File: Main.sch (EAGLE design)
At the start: 18 parts, among them X1 736880-49, X2 736880-49

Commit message: [rm]いったん全部消去
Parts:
- removed C1, C2, C3, C4, C5, C6: (no value), capacitor-wima:C10/5
- removed R1, R2, R3, R4, R5, R6: (no value), rcl:R-EU_0207/5V
- removed TR1, TR2: 166L8, trafo-hammondmfg:166L8
- removed V1, V2: (no value), VacuumTube:6BQ5-P
- removed X1, X2: 736880-49, con-conrad:736880-49
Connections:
- removed net GND: C2.2, C4.2, C5.2, C6.2, R1.1, R2.1, R3.1, R5.1
- removed net N$1: C2.1, R5.2, V2G$1.PK
- removed net N$12: C1.1, X2.2
- removed net N$2: C6.1, R6.2, V2G$1.PSG
- removed net N$3: C3.2, R2.2, V1G$1.PG
- removed net N$4: C1.2, R1.2, V2G$1.PG
- removed net N$5: TR2.BLK@1, V1G$1.PA
- removed net N$6: TR1.BLK@1, V2G$1.PA
- removed net N$7: C3.1, X1.2
- removed net N$8: C4.1, R3.2, V1G$1.PK
- removed net N$9: C5.1, R4.2, V1G$1.PSG
- removed net VCC: R4.1, R6.1, TR1.BLK@2, TR2.BLK@2

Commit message: [add]全回路作成
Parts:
- added C1, C2, C3, C6, C7, C8: 0.1u, VacuumTube:C
- added C10, C5: 10u, VacuumTube:C
- added C4, C9: 170, VacuumTube:C
- added JP1, JP2, JP3, JP4, JP5, JP6: (no value), VacuumTube:PINHD-1X2
- added R1, R10, R16, R7: 220k, VacuumTube:RESISTOR2
- added R11, R2: 3.83k, VacuumTube:RESISTOR2
- added R12, R3: 50k, VacuumTube:RESISTOR2
- added R13, R4: 1M, VacuumTube:RESISTOR2
- added R14, R5: 1.5k, VacuumTube:RESISTOR2
- added R15, R6: 100k, VacuumTube:RESISTOR2
- added R17, R8: 220u, VacuumTube:RESISTOR2
- added R18, R9: 2k, VacuumTube:RESISTOR2
- added V1, V3: (no value), VacuumTube:AT-MT9P(12AX7)
- added V2, V4: (no value), VacuumTube:AT-MT9P(6BQ5)
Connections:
- new net GND: C10.2, C4.2, C5.2, C9.2, JP1.1, JP2.1, JP3.1, JP4.1, R1.1, R10.1, R11.1, R15.1, R16.2, R17.2, R2.1, R6.1, R7.2, R8.2, V1C.H2, V2B.H2, V3C.H2, V4B.H2
- new net N$1: R3.1, V1A.TA
- new net N$10: C2.1
- new net N$11: V1C.H3, V3C.H3
- new net N$12: C3.1
- new net N$13: C3.2, R7.1, V2A.PG
- new net N$14: C4.1, R8.1, V2A.PK
- new net N$15: V2A.PA
- new net N$16: JP5.1
- new net N$17: C5.1, R9.1, V2A.PSG
- new net N$18: JP6.1
- new net N$19: R12.1, V3A.TA
- new net N$2: R2.2, V1A.TK
- new net N$20: R11.2, V3A.TK
- new net N$21: C6.2, R10.2, V3A.TG
- new net N$22: C6.1
- new net N$23: R14.2, V3B.TK
- new net N$24: R13.1, R14.1, R15.2
- new net N$25: C7.2, R13.2, V3B.TG
- new net N$26: C7.1
- new net N$27: C8.1
- new net N$28: C8.2, R16.1, V4A.PG
- new net N$29: C9.1, R17.1, V4A.PK
- new net N$3: JP2.2
- new net N$30: V4A.PA
- new net N$31: C10.1, R18.1, V4A.PSG
- new net N$4: JP1.2
- new net N$5: C1.2, R1.2, V1A.TG
- new net N$6: R5.2, V1B.TK
- new net N$7: C1.1
- new net N$8: R4.1, R5.1, R6.2
- new net N$9: C2.2, R4.2, V1B.TG
- new net VCC: JP3.2, JP5.2, JP6.2, R12.2, R18.2, R3.2, R9.2, V1B.TA, V3B.TA
- new net VCC/2: JP4.2, V1C.H1, V2B.H1, V3C.H1, V4B.H1
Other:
- note added: "FIRST_OUT1"
- note added: "FIRST_OUT2"
- note added: "INPUT1"
- note added: "INPUT2"
- note added: "SECOND_OUT1"
- note added: "SECOND_OUT2"
- note added: "THIRD_OUT1"
- note added: "THIRD_OUT2"

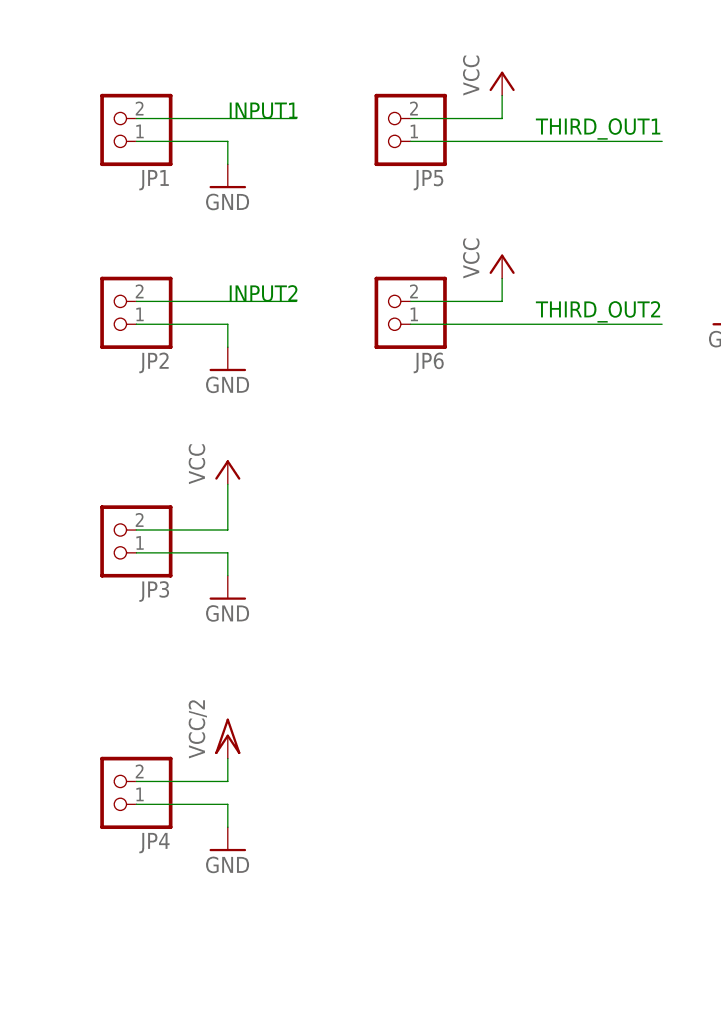
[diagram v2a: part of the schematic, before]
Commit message: [fix]ピンのラベルを編集
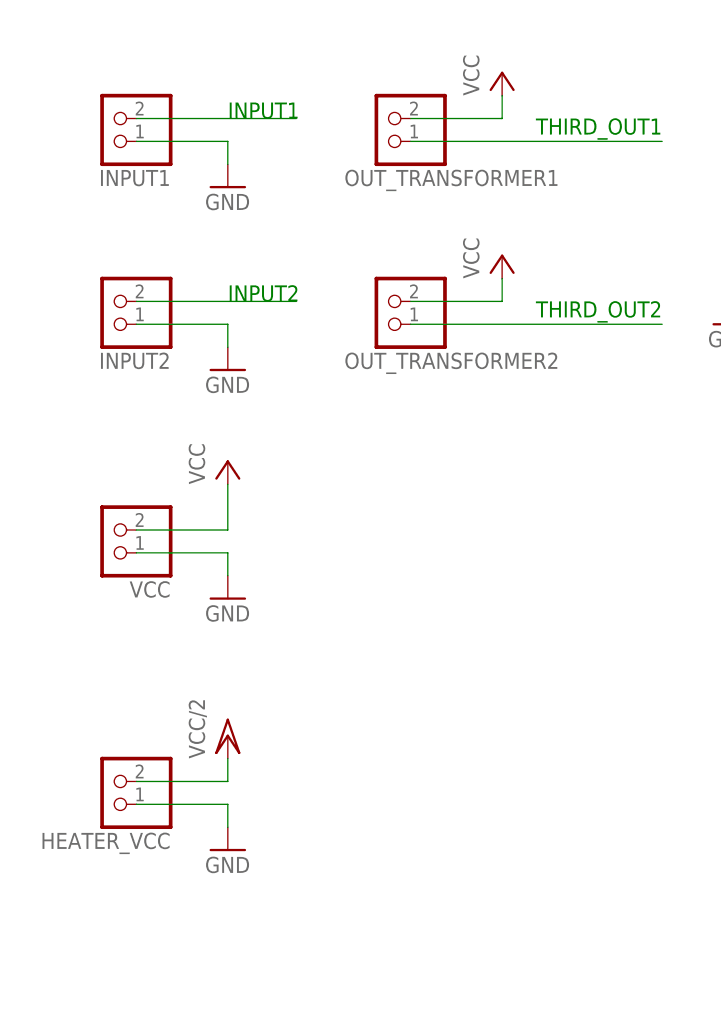
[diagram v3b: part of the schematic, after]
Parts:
- renumbered JP1 to INPUT1, JP2 to INPUT2, JP3 to VCC, JP4 to HEATER_VCC, JP5 to OUT_TRANSFORMER1, JP6 to OUT_TRANSFORMER2
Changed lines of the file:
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@@
 </classes>
 <parts>
-<part name="JP1" library="VacuumTube" library_urn="urn:adsk.eagle:library:8044196" deviceset="PINHD-1X2" device="" package3d_urn="urn:adsk.eagle:package:22435/2"/>
-<part name="JP2" library="VacuumTube" library_urn="urn:adsk.eagle:library:8044196" deviceset="PINHD-1X2" device="" package3d_urn="urn:adsk.eagle:package:22435/2"/>
+<part name="INPUT1" library="VacuumTube" library_urn="urn:adsk.eagle:library:8044196" deviceset="PINHD-1X2" device="" package3d_urn="urn:adsk.eagle:package:22435/2"/>
+<part name="INPUT2" library="VacuumTube" library_urn="urn:adsk.eagle:library:8044196" deviceset="PINHD-1X2" device="" package3d_urn="urn:adsk.eagle:package:22435/2"/>
 <part name="GND1" library="VacuumTube" library_urn="urn:adsk.eagle:library:8044196" deviceset="GND" device=""/>
 <part name="GND2" library="VacuumTube" library_urn="urn:adsk.eagle:library:8044196" deviceset="GND" device=""/>
-<part name="JP3" library="VacuumTube" library_urn="urn:adsk.eagle:library:8044196" deviceset="PINHD-1X2" device="" package3d_urn="urn:adsk.eagle:package:22435/2"/>
+<part name="VCC" library="VacuumTube" library_urn="urn:adsk.eagle:library:8044196" deviceset="PINHD-1X2" device="" package3d_urn="urn:adsk.eagle:package:22435/2"/>
 <part name="GND3" library="VacuumTube" library_urn="urn:adsk.eagle:library:8044196" deviceset="GND" device=""/>
 <part name="P+1" library="VacuumTube" library_urn="urn:adsk.eagle:library:8044196" deviceset="VCC" device=""/>
-<part name="JP4" library="VacuumTube" library_urn="urn:adsk.eagle:library:8044196" deviceset="PINHD-1X2" device="" package3d_urn="urn:adsk.eagle:package:22435/2"/>
+<part name="HEATER_VCC" library="VacuumTube" library_urn="urn:adsk.eagle:library:8044196" deviceset="PINHD-1X2" device="" package3d_urn="urn:adsk.eagle:package:22435/2"/>
 <part name="GND4" library="VacuumTube" library_urn="urn:adsk.eagle:library:8044196" deviceset="GND" device=""/>
 <part name="P+2" library="VacuumTube" library_urn="urn:adsk.eagle:library:8044196" deviceset="VCC/2" device=""/>
@@
 <part name="P+8" library="VacuumTube" library_urn="urn:adsk.eagle:library:8044196" deviceset="VCC" device=""/>
 <part name="GND13" library="VacuumTube" library_urn="urn:adsk.eagle:library:8044196" deviceset="GND" device=""/>
-<part name="JP5" library="VacuumTube" library_urn="urn:adsk.eagle:library:8044196" deviceset="PINHD-1X2" device="" package3d_urn="urn:adsk.eagle:package:22435/2"/>
+<part name="OUT_TRANSFORMER1" library="VacuumTube" library_urn="urn:adsk.eagle:library:8044196" deviceset="PINHD-1X2" device="" package3d_urn="urn:adsk.eagle:package:22435/2"/>
 <part name="P+9" library="VacuumTube" library_urn="urn:adsk.eagle:library:8044196" deviceset="VCC" device=""/>
 <part name="R9" library="VacuumTube" library_urn="urn:adsk.eagle:library:8044196" deviceset="RESISTOR2" device="" package3d_urn="urn:adsk.eagle:package:8969348/1" value="2k"/>
-<part name="JP6" library="VacuumTube" library_urn="urn:adsk.eagle:library:8044196" deviceset="PINHD-1X2" device="" package3d_urn="urn:adsk.eagle:package:22435/2"/>
+<part name="OUT_TRANSFORMER2" library="VacuumTube" library_urn="urn:adsk.eagle:library:8044196" deviceset="PINHD-1X2" device="" package3d_urn="urn:adsk.eagle:package:22435/2"/>
 <part name="P+10" library="VacuumTube" library_urn="urn:adsk.eagle:library:8044196" deviceset="VCC" device=""/>
 <part name="GND14" library="VacuumTube" library_urn="urn:adsk.eagle:library:8044196" deviceset="GND" device=""/>
@@
 </plain>
 <instances>
-<instance part="JP1" gate="G$1" x="0" y="93.98" smashed="yes" rot="R180">
+<instance part="INPUT1" gate="G$1" x="0" y="93.98" smashed="yes" rot="R180">
 <attribute name="NAME" x="6.35" y="88.265" size="1.778" layer="95" rot="R180"/>
 <attribute name="VALUE" x="6.35" y="99.06" size="1.778" layer="96" rot="R180"/>
 </instance>
-<instance part="JP2" gate="G$1" x="0" y="73.66" smashed="yes" rot="R180">
+<instance part="INPUT2" gate="G$1" x="0" y="73.66" smashed="yes" rot="R180">
 <attribute name="NAME" x="6.35" y="67.945" size="1.778" layer="95" rot="R180"/>
 <attribute name="VALUE" x="6.35" y="78.74" size="1.778" layer="96" rot="R180"/>
@@
 <attribute name="VALUE" x="10.16" y="63.5" size="1.778" layer="96"/>
 </instance>
-<instance part="JP3" gate="G$1" x="0" y="48.26" smashed="yes" rot="R180">
+<instance part="VCC" gate="G$1" x="0" y="48.26" smashed="yes" rot="R180">
 <attribute name="NAME" x="6.35" y="42.545" size="1.778" layer="95" rot="R180"/>
 <attribute name="VALUE" x="6.35" y="53.34" size="1.778" layer="96" rot="R180"/>
@@
 <attribute name="VALUE" x="10.16" y="53.34" size="1.778" layer="96" rot="R90"/>
 </instance>
-<instance part="JP4" gate="G$1" x="0" y="20.32" smashed="yes" rot="R180">
+<instance part="HEATER_VCC" gate="G$1" x="0" y="20.32" smashed="yes" rot="R180">
 <attribute name="NAME" x="6.35" y="14.605" size="1.778" layer="95" rot="R180"/>
 <attribute name="VALUE" x="6.35" y="25.4" size="1.778" layer="96" rot="R180"/>
@@
 <attribute name="VALUE" x="350.52" y="45.72" size="1.778" layer="96"/>
 </instance>
-<instance part="JP5" gate="G$1" x="30.48" y="93.98" smashed="yes" rot="R180">
-<attribute name="NAME" x="36.83" y="88.265" size="1.778" layer="95" rot="R180"/>
+<instance part="OUT_TRANSFORMER1" gate="G$1" x="30.48" y="93.98" smashed="yes" rot="R180">
+<attribute name="NAME" x="49.53" y="88.265" size="1.778" layer="95" rot="R180"/>
 <attribute name="VALUE" x="36.83" y="99.06" size="1.778" layer="96" rot="R180"/>
 </instance>
@@
 <attribute name="VALUE" x="356.362" y="92.71" size="1.778" layer="96" rot="R90"/>
 </instance>
-<instance part="JP6" gate="G$1" x="30.48" y="73.66" smashed="yes" rot="R180">
-<attribute name="NAME" x="36.83" y="67.945" size="1.778" layer="95" rot="R180"/>
+<instance part="OUT_TRANSFORMER2" gate="G$1" x="30.48" y="73.66" smashed="yes" rot="R180">
+<attribute name="NAME" x="49.53" y="67.945" size="1.778" layer="95" rot="R180"/>
 <attribute name="VALUE" x="36.83" y="78.74" size="1.778" layer="96" rot="R180"/>
 </instance>
@@
 <net name="GND" class="0">
 <segment>
-<pinref part="JP1" gate="G$1" pin="1"/>
+<pinref part="INPUT1" gate="G$1" pin="1"/>
 <wire x1="2.54" y1="91.44" x2="12.7" y2="91.44" width="0.1524" layer="91"/>
 <pinref part="GND1" gate="1" pin="GND"/>
@@
 </segment>
 <segment>
-<pinref part="JP2" gate="G$1" pin="1"/>
+<pinref part="INPUT2" gate="G$1" pin="1"/>
 <wire x1="2.54" y1="71.12" x2="12.7" y2="71.12" width="0.1524" layer="91"/>
 <pinref part="GND2" gate="1" pin="GND"/>
@@
 <segment>
 <pinref part="GND3" gate="1" pin="GND"/>
-<pinref part="JP3" gate="G$1" pin="1"/>
+<pinref part="VCC" gate="G$1" pin="1"/>
 <wire x1="12.7" y1="43.18" x2="12.7" y2="45.72" width="0.1524" layer="91"/>
 <wire x1="12.7" y1="45.72" x2="2.54" y2="45.72" width="0.1524" layer="91"/>
@@
 <wire x1="12.7" y1="15.24" x2="12.7" y2="17.78" width="0.1524" layer="91"/>
 <wire x1="12.7" y1="17.78" x2="2.54" y2="17.78" width="0.1524" layer="91"/>
-<pinref part="JP4" gate="G$1" pin="1"/>
+<pinref part="HEATER_VCC" gate="G$1" pin="1"/>
 </segment>
 <segment>
@@
 <net name="N$3" class="0">
 <segment>
-<pinref part="JP2" gate="G$1" pin="2"/>
+<pinref part="INPUT2" gate="G$1" pin="2"/>
 <wire x1="2.54" y1="73.66" x2="20.32" y2="73.66" width="0.1524" layer="91"/>
 </segment>
@@
 <net name="N$4" class="0">
 <segment>
-<pinref part="JP1" gate="G$1" pin="2"/>
+<pinref part="INPUT1" gate="G$1" pin="2"/>
 <wire x1="2.54" y1="93.98" x2="20.32" y2="93.98" width="0.1524" layer="91"/>
 </segment>
@@
 <segment>
 <pinref part="P+1" gate="VCC" pin="VCC"/>
-<pinref part="JP3" gate="G$1" pin="2"/>
+<pinref part="VCC" gate="G$1" pin="2"/>
 <wire x1="12.7" y1="53.34" x2="12.7" y2="48.26" width="0.1524" layer="91"/>
 <wire x1="12.7" y1="48.26" x2="2.54" y2="48.26" width="0.1524" layer="91"/>
@@
 <pinref part="P+9" gate="VCC" pin="VCC"/>
 <wire x1="43.18" y1="96.52" x2="43.18" y2="93.98" width="0.1524" layer="91"/>
-<pinref part="JP5" gate="G$1" pin="2"/>
+<pinref part="OUT_TRANSFORMER1" gate="G$1" pin="2"/>
 <wire x1="43.18" y1="93.98" x2="33.02" y2="93.98" width="0.1524" layer="91"/>
 </segment>
@@
 <pinref part="P+10" gate="VCC" pin="VCC"/>
 <wire x1="43.18" y1="76.2" x2="43.18" y2="73.66" width="0.1524" layer="91"/>
-<pinref part="JP6" gate="G$1" pin="2"/>
+<pinref part="OUT_TRANSFORMER2" gate="G$1" pin="2"/>
 <wire x1="43.18" y1="73.66" x2="33.02" y2="73.66" width="0.1524" layer="91"/>
 </segment>
@@
 <pinref part="P+2" gate="G$1" pin="VCC/2"/>
 <wire x1="12.7" y1="22.86" x2="12.7" y2="20.32" width="0.1524" layer="91"/>
-<pinref part="JP4" gate="G$1" pin="2"/>
+<pinref part="HEATER_VCC" gate="G$1" pin="2"/>
 <wire x1="12.7" y1="20.32" x2="2.54" y2="20.32" width="0.1524" layer="91"/>
 </segment>
@@
 <net name="N$16" class="0">
 <segment>
-<pinref part="JP5" gate="G$1" pin="1"/>
+<pinref part="OUT_TRANSFORMER1" gate="G$1" pin="1"/>
 <wire x1="33.02" y1="91.44" x2="60.96" y2="91.44" width="0.1524" layer="91"/>
 </segment>
@@
 <net name="N$18" class="0">
 <segment>
-<pinref part="JP6" gate="G$1" pin="1"/>
+<pinref part="OUT_TRANSFORMER2" gate="G$1" pin="1"/>
 <wire x1="33.02" y1="71.12" x2="60.96" y2="71.12" width="0.1524" layer="91"/>
 </segment>

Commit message: [fix]基板に絶望している
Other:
- moved on the sheet: V1C, V2A, V2B, V3C, V4A, V4B
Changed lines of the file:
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@@
 <part name="C1" library="VacuumTube" library_urn="urn:adsk.eagle:library:8044196" deviceset="C" device="" package3d_urn="urn:adsk.eagle:package:8969349/1" value="0.1u"/>
 <part name="C2" library="VacuumTube" library_urn="urn:adsk.eagle:library:8044196" deviceset="C" device="" package3d_urn="urn:adsk.eagle:package:8969349/1" value="0.1u"/>
-<part name="V1" library="VacuumTube" library_urn="urn:adsk.eagle:library:8044196" deviceset="AT-MT9P(12AX7)" device="" package3d_urn="urn:adsk.eagle:package:8092351/9"/>
-<part name="V2" library="VacuumTube" library_urn="urn:adsk.eagle:library:8044196" deviceset="AT-MT9P(6BQ5)" device="" package3d_urn="urn:adsk.eagle:package:8092351/9"/>
+<part name="V1" library="VacuumTube" library_urn="urn:adsk.eagle:library:8044196" deviceset="AT-MT9P(12AX7)" device="" package3d_urn="urn:adsk.eagle:package:8092351/10"/>
+<part name="V2" library="VacuumTube" library_urn="urn:adsk.eagle:library:8044196" deviceset="AT-MT9P(6BQ5)" device="" package3d_urn="urn:adsk.eagle:package:8092351/10"/>
 <part name="P+7" library="VacuumTube" library_urn="urn:adsk.eagle:library:8044196" deviceset="VCC/2" device=""/>
 <part name="GND8" library="VacuumTube" library_urn="urn:adsk.eagle:library:8044196" deviceset="GND" device=""/>
@@
 <part name="C6" library="VacuumTube" library_urn="urn:adsk.eagle:library:8044196" deviceset="C" device="" package3d_urn="urn:adsk.eagle:package:8969349/1" value="0.1u"/>
 <part name="C7" library="VacuumTube" library_urn="urn:adsk.eagle:library:8044196" deviceset="C" device="" package3d_urn="urn:adsk.eagle:package:8969349/1" value="0.1u"/>
-<part name="V3" library="VacuumTube" library_urn="urn:adsk.eagle:library:8044196" deviceset="AT-MT9P(12AX7)" device="" package3d_urn="urn:adsk.eagle:package:8092351/9"/>
-<part name="V4" library="VacuumTube" library_urn="urn:adsk.eagle:library:8044196" deviceset="AT-MT9P(6BQ5)" device="" package3d_urn="urn:adsk.eagle:package:8092351/9"/>
+<part name="V3" library="VacuumTube" library_urn="urn:adsk.eagle:library:8044196" deviceset="AT-MT9P(12AX7)" device="" package3d_urn="urn:adsk.eagle:package:8092351/10"/>
+<part name="V4" library="VacuumTube" library_urn="urn:adsk.eagle:library:8044196" deviceset="AT-MT9P(6BQ5)" device="" package3d_urn="urn:adsk.eagle:package:8092351/10"/>
 <part name="P+15" library="VacuumTube" library_urn="urn:adsk.eagle:library:8044196" deviceset="VCC/2" device=""/>
 <part name="GND18" library="VacuumTube" library_urn="urn:adsk.eagle:library:8044196" deviceset="GND" device=""/>

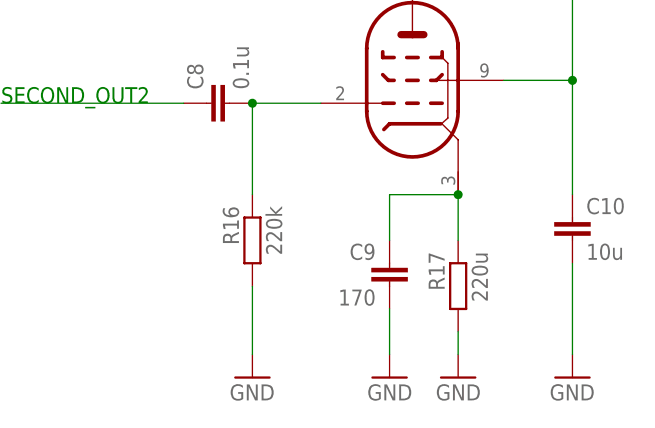
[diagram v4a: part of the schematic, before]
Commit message: [fix]重大な欠陥を直した
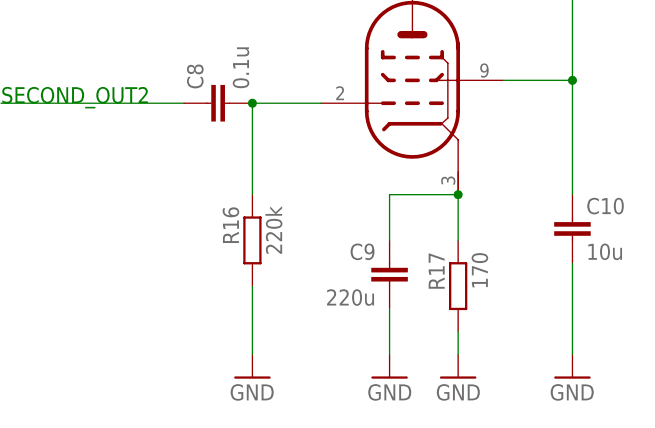
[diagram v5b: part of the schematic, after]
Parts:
- C9: value 170 -> 220u
- R17: value 220u -> 170
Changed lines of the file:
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@@
 <setting verticaltext="up"/>
 </settings>
-<grid distance="0.1" unitdist="inch" unit="inch" style="lines" multiple="1" display="yes" altdistance="0.01" altunitdist="inch" altunit="inch"/>
+<grid distance="0.1" unitdist="inch" unit="inch" style="lines" multiple="1" display="no" altdistance="0.01" altunitdist="inch" altunit="inch"/>
 <layers>
 <layer number="1" name="Top" color="4" fill="9" visible="no" active="no"/>
@@
 <part name="GND18" library="VacuumTube" library_urn="urn:adsk.eagle:library:8044196" deviceset="GND" device=""/>
 <part name="C8" library="VacuumTube" library_urn="urn:adsk.eagle:library:8044196" deviceset="C" device="" package3d_urn="urn:adsk.eagle:package:8969349/1" value="0.1u"/>
-<part name="C9" library="VacuumTube" library_urn="urn:adsk.eagle:library:8044196" deviceset="C" device="" package3d_urn="urn:adsk.eagle:package:8969349/1" value="170"/>
+<part name="C9" library="VacuumTube" library_urn="urn:adsk.eagle:library:8044196" deviceset="C" device="" package3d_urn="urn:adsk.eagle:package:8969349/1" value="220u"/>
 <part name="GND19" library="VacuumTube" library_urn="urn:adsk.eagle:library:8044196" deviceset="GND" device=""/>
 <part name="GND20" library="VacuumTube" library_urn="urn:adsk.eagle:library:8044196" deviceset="GND" device=""/>
 <part name="R16" library="VacuumTube" library_urn="urn:adsk.eagle:library:8044196" deviceset="RESISTOR2" device="" package3d_urn="urn:adsk.eagle:package:8969348/1" value="220k"/>
-<part name="R17" library="VacuumTube" library_urn="urn:adsk.eagle:library:8044196" deviceset="RESISTOR2" device="" package3d_urn="urn:adsk.eagle:package:8969348/1" value="220u"/>
+<part name="R17" library="VacuumTube" library_urn="urn:adsk.eagle:library:8044196" deviceset="RESISTOR2" device="" package3d_urn="urn:adsk.eagle:package:8969348/1" value="170"/>
 <part name="GND21" library="VacuumTube" library_urn="urn:adsk.eagle:library:8044196" deviceset="GND" device=""/>
 <part name="C10" library="VacuumTube" library_urn="urn:adsk.eagle:library:8044196" deviceset="C" device="" package3d_urn="urn:adsk.eagle:package:8969349/1" value="10u"/>

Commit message: [fix]重大な欠陥
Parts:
- C4: value 170 -> 220u
- R8: value 220u -> 170
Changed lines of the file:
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@@
 <part name="GND8" library="VacuumTube" library_urn="urn:adsk.eagle:library:8044196" deviceset="GND" device=""/>
 <part name="C3" library="VacuumTube" library_urn="urn:adsk.eagle:library:8044196" deviceset="C" device="" package3d_urn="urn:adsk.eagle:package:8969349/1" value="0.1u"/>
-<part name="C4" library="VacuumTube" library_urn="urn:adsk.eagle:library:8044196" deviceset="C" device="" package3d_urn="urn:adsk.eagle:package:8969349/1" value="170"/>
+<part name="C4" library="VacuumTube" library_urn="urn:adsk.eagle:library:8044196" deviceset="C" device="" package3d_urn="urn:adsk.eagle:package:8969349/1" value="220u"/>
 <part name="GND10" library="VacuumTube" library_urn="urn:adsk.eagle:library:8044196" deviceset="GND" device=""/>
 <part name="GND11" library="VacuumTube" library_urn="urn:adsk.eagle:library:8044196" deviceset="GND" device=""/>
 <part name="R7" library="VacuumTube" library_urn="urn:adsk.eagle:library:8044196" deviceset="RESISTOR2" device="" package3d_urn="urn:adsk.eagle:package:8969348/1" value="220k"/>
-<part name="R8" library="VacuumTube" library_urn="urn:adsk.eagle:library:8044196" deviceset="RESISTOR2" device="" package3d_urn="urn:adsk.eagle:package:8969348/1" value="220u"/>
+<part name="R8" library="VacuumTube" library_urn="urn:adsk.eagle:library:8044196" deviceset="RESISTOR2" device="" package3d_urn="urn:adsk.eagle:package:8969348/1" value="170"/>
 <part name="GND12" library="VacuumTube" library_urn="urn:adsk.eagle:library:8044196" deviceset="GND" device=""/>
 <part name="C5" library="VacuumTube" library_urn="urn:adsk.eagle:library:8044196" deviceset="C" device="" package3d_urn="urn:adsk.eagle:package:8969349/1" value="10u"/>
